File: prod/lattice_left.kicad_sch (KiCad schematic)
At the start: 84 parts, among them J1 USB_C_Receptacle, J2 USB_C_Receptacle, J3 Conn_01x05, SW1 SW_Push, SW2 SW_Push, U1 RP2040, U2 XC6206PxxxMR, U3 USBLC6-2SC6, U4 W25Q128JVS, Y1 12MHz

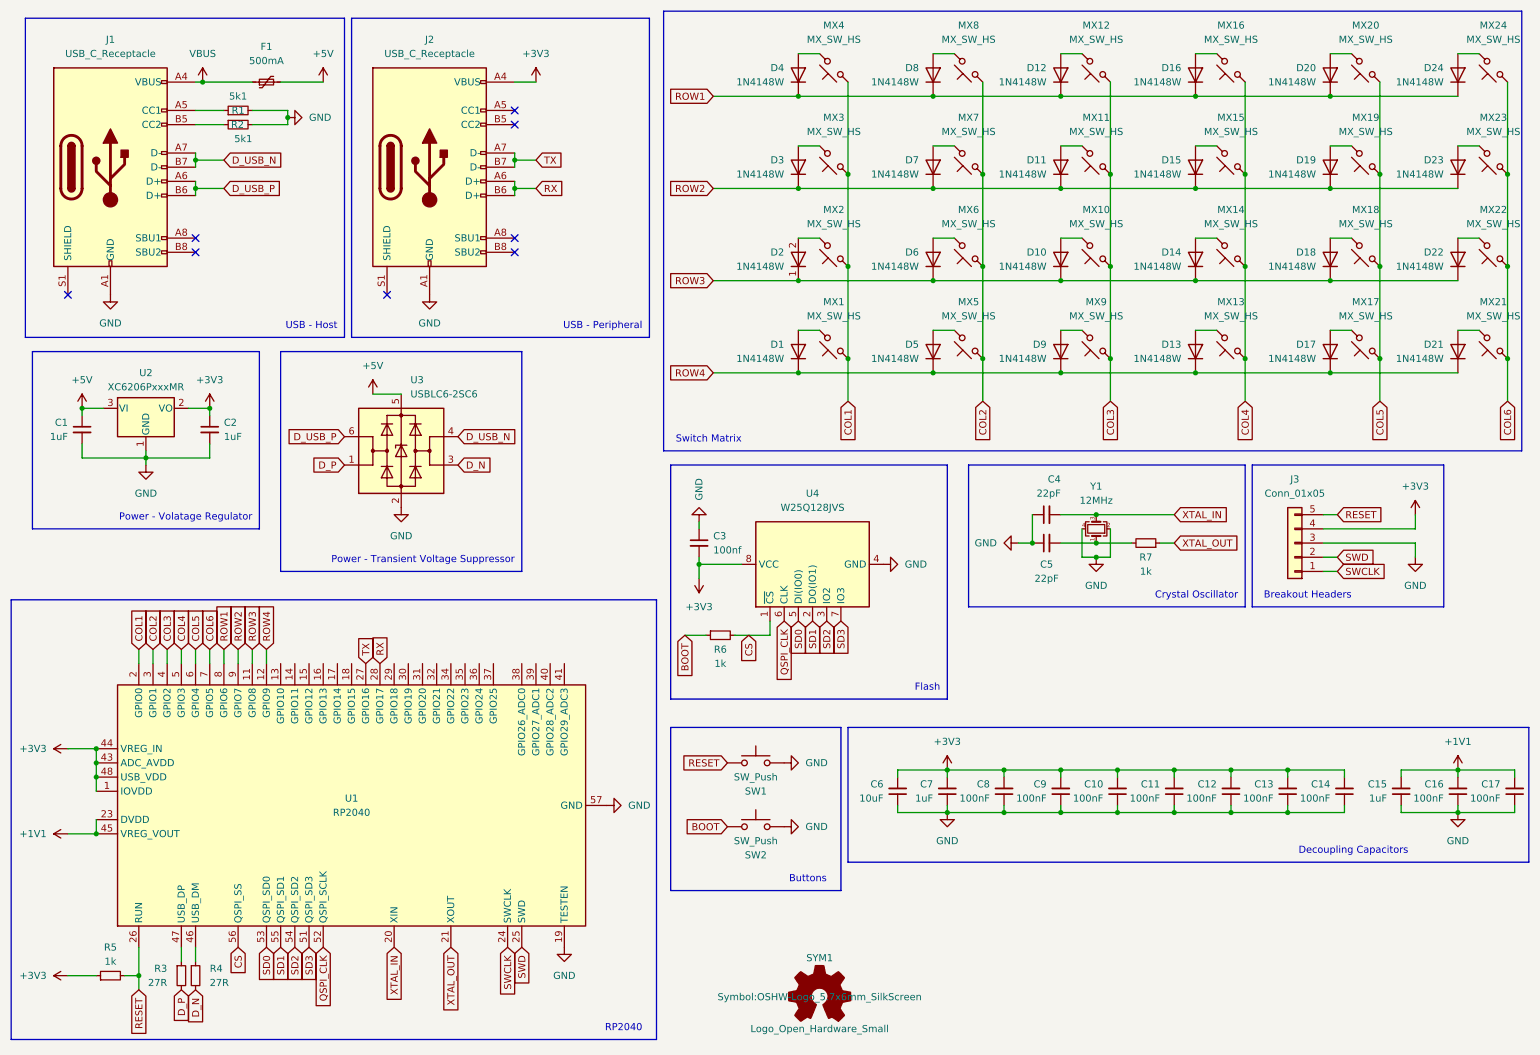
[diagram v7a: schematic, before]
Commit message: preoject-specific 3dmodels and footprints
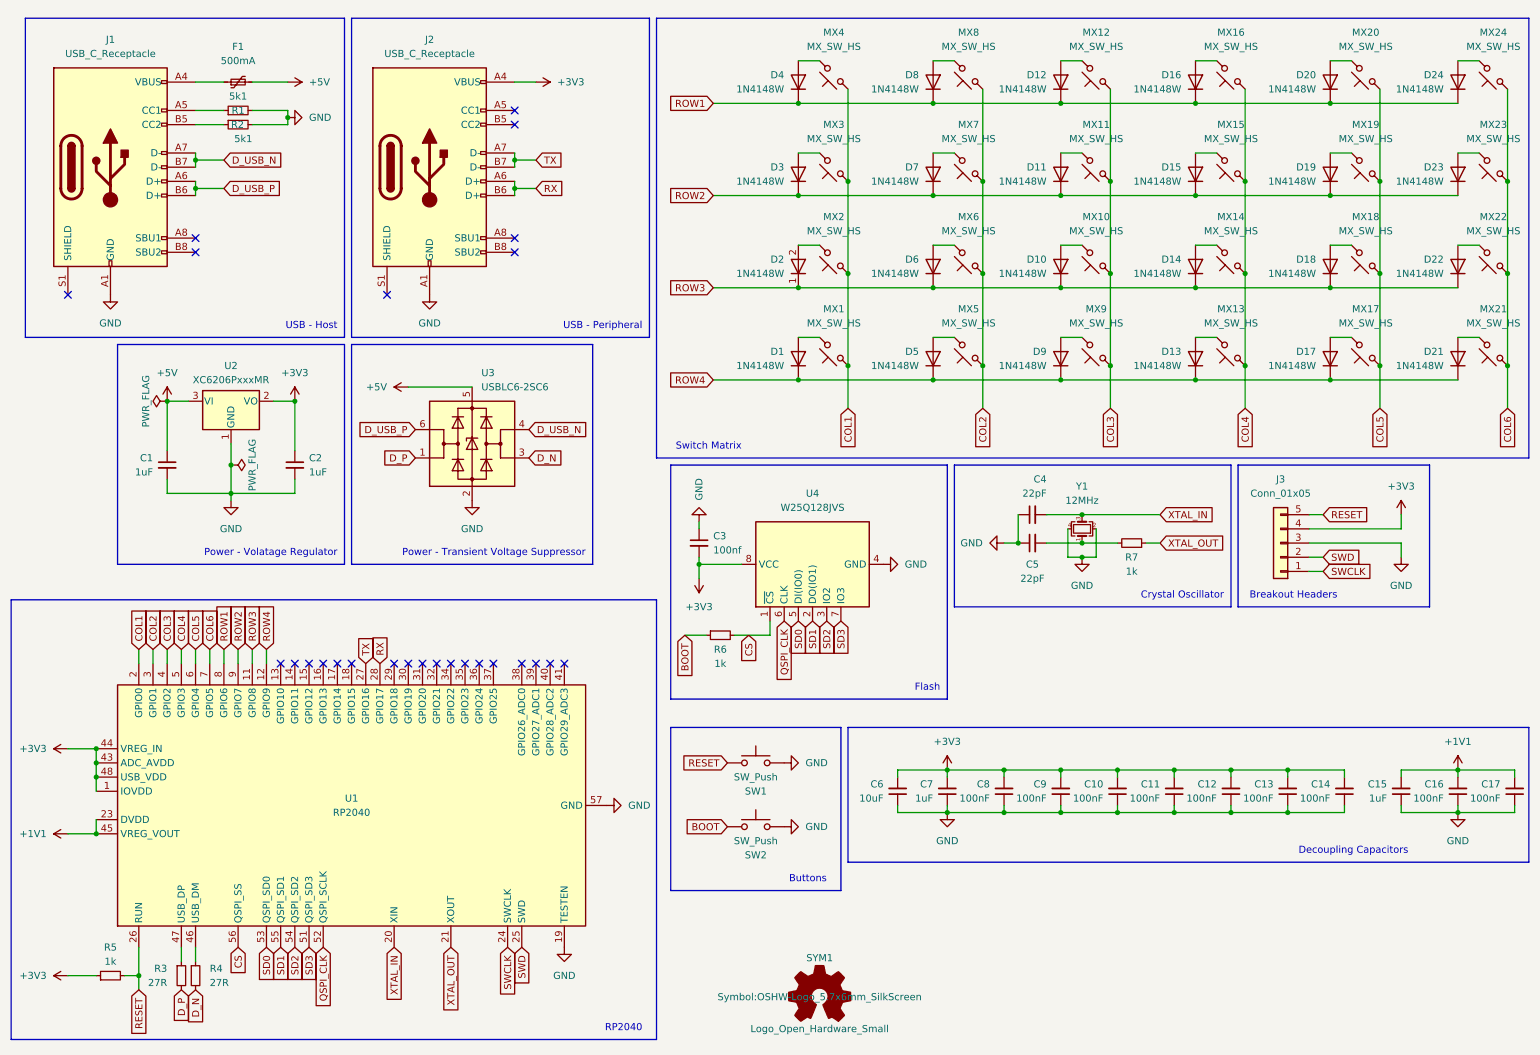
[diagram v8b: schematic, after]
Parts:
- J1, J2: footprint Connector_USB:USB_C_Receptacle_HRO_TYPE-C-31-M-12 -> lattice:USB_C_Receptacle_HRO_TYPE-C-31-M-12
- J3: footprint Connector_PinSocket_2.54mm:PinSocket_1x05_P2.54mm_Vertical -> lattice:PinHeader_1x05_P2.54mm_Vertical
- SW1, SW2: footprint Button_Switch_SMD:SW_SPST_SKQG_WithStem -> lattice:SW_SPST_SKQG_WithStem
- U2: footprint Package_TO_SOT_SMD:SOT-23-3 -> lattice:SOT-23-3
- U4: footprint Package_SO:SOIC-8_5.23x5.23mm_P1.27mm -> lattice:SOIC-8_5.23x5.23mm_P1.27mm
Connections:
- net VBUS: no longer names the net of F1.1, J1.A4 (VBUS), J1.A9 (VBUS), J1.B4 (VBUS), J1.B9 (VBUS)
- no-connect marks 8 -> 26
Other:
- moved on the sheet: C1, C2, C4, C5, D1, D10, D11, D12, D13, D14, D15, D16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
